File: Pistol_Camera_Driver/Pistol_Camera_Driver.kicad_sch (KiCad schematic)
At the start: 3 parts

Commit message: v0.2 Circuit has been complemented
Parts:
- added C? (x10): C, symbol Device:C
- added D? (x2): WHITE_LED, symbol Device:LED
- added D? (x2): UV_LED, symbol Device:LED
- added J? (x5): Screw_Terminal_01x02, symbol Connector:Screw_Terminal_01x02
- added J?: Screw_Terminal_01x03, symbol Connector:Screw_Terminal_01x03
- added J?: Conn_01x08, symbol Connector_Generic:Conn_01x08
- added M?: Fan, symbol Motor:Fan
- added R? (x15): R, Resistor_SMD:R_0603_1608Metric_Pad0.98x0.95mm_HandSolder, symbol Device:R
- added U?: LM7805_TO220, Package_TO_SOT_THT:TO-220-3_Vertical, symbol Regulator_Linear:LM7805_TO220
- added U?: LM317_TO-263, Package_TO_SOT_SMD:TO-263-2, symbol Regulator_Linear:LM317_TO-263
- added U? (x2): LDD-700L, Converter_DCDC:Converter_DCDC_Murata_NCS1SxxxxSC_THT, symbol Converter_DCDC:NCS1S1203SC
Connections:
- net GND: now reaches U?.13 (GND)
- net GND: now also U?.19 (GP14), U?.21 (GND), U?.21 (GND), U?.23 (GND), U?.25 (GND), U?.25 (GND), U?.28 (GND), U?.3 (GND), U?.33 (AGND), U?.38 (GND), U?.8 (GND), C?.2, C?.2, C?.2, C?.2, J?.2 (Pin_2), J?.2 (Pin_2), J?.2 (Pin_2), J?.3 (Pin_3), M?.2 (-), R?.1, R?.1, R?.1, R?.1, R?.1, R?.1, R?.1, R?.1, R?.2, R?.2, U?.1 (-VIN), U?.1 (-VIN), U?.2 (GND)
- net +5V: now reaches U?.39 (VSYS)
- net +5V: now also C?.1, C?.1, U?.3 (VI), U?.3 (VO)
- net Strobe Input: now reaches U?.4 (GP2)
- net Strobe Input: now also J?.1 (Pin_1)
- net PWM_UV: now reaches U?.7 (GP5/SCL)
- net PWM_UV: now also J?.1 (Pin_1), R?.1, U?.3 (Control)
- net PWM_WHITE: now reaches U?.9 (GP6)
- net PWM_WHITE: now also J?.2 (Pin_2), U?.3 (Control)
- net MOTORS_nSLEEP: now reaches U?.1 (nSLEEP)
- net MOTORS_nSLEEP: now also U?.1 (nSLEEP), R?.2, R?.2
- net nEN1: now reaches U?.10 (nENBL)
- net STEP1: now reaches U?.11 (STEP)
- net DIR1: now reaches U?.12 (DIR)
- net M0_1: now reaches U?.13 (M0)
- net M1_1: now reaches U?.14 (M1)
- net at U?.15 (CONFIG): now also U?.20 (VINT) (x2)
- net at U?.16 (nFAULT): now also R?.2 (x2)
- net +3V3: now reaches U?.18 (VM)
- net +3V3: now also U?.18 (VM), U?.19 (VM), U?.19 (VM), C?.1, R?.1, R?.1, R?.1, R?.1, R?.1, U?.2 (VO)
- net at U?.2 (BDECAY): now also R?.2 (x2)
- net at U?.22 (AVREF): now also U?.23 (BVREF), U?.24 (VREFO) (x2)
- net at U?.3 (ADECAY): now also R?.2 (x2)
- net AOUT1_1: now reaches U?.4 (AOUT1)
- net at U?.5 (AISEN): now also R?.2 (x2)
- net AOUT2_1: now reaches U?.6 (AOUT2)
- net BOUT2_1: now reaches U?.7 (BOUT2)
- net at U?.8 (BISEN): now also R?.2 (x2)
- net BOUT1_2: now reaches U?.9 (BOUT1)
- net BOUT1_2: now also U?.9 (BOUT1)
- net nEN2: now reaches U?.10 (nENBL)
- net STEP2: now reaches U?.11 (STEP)
- net DIR2: now reaches U?.12 (DIR)
- net M0_2: now reaches U?.13 (M0)
- net M1_2: now reaches U?.14 (M1)
- net AOUT1_2: now reaches U?.4 (AOUT1)
- net AOUT2_2: now reaches U?.6 (AOUT2)
- net BOUT2_2: now reaches U?.7 (BOUT2)
- new net: D?.2 (A), J?.1 (Pin_1), U?.6 (+VOUT) (x2)
- new net: D?.1 (K), J?.2 (Pin_2), U?.7 (-VOUT) (x2)
- new net: D?.1 (K), D?.2 (A) (x2)
- new net: R?.1, R?.2, U?.1 (ADJ)
- new net +12V: C?.1, J?.1 (Pin_1), J?.1 (Pin_1), M?.1 (+), U?.1 (VI), U?.2 (+VIN), U?.2 (+VIN)
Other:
- moved on the sheet: U?

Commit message: v0.3 Circuit except the joystick has been completed
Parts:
- added C? (x2): C_Polarized, symbol Device:C_Polarized
- added J?: Conn_01x04_Female, Connector_PinSocket_2.54mm:PinSocket_1x04_P2.54mm_Vertical, symbol Connector:Conn_01x04_Female
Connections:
- net +3V3: now also C?.1, C?.2, C?.2, C?.2, C?.1, C?.1
- net +5V: now also J?.1 (Pin_1)
- net AOUT1_1: now also J?.4 (Pin_4)
- net AOUT1_2: now also J?.2 (Pin_2)
- net AOUT2_1: now also J?.3 (Pin_3)
- net AOUT2_2: now also J?.1 (Pin_1)
- net BOUT1_1: now also J?.5 (Pin_5), U?.9 (BOUT1)
- net BOUT1_2: now also J?.8 (Pin_8); no longer U?.9 (BOUT1)
- net BOUT2_1: now also J?.6 (Pin_6)
- net BOUT2_2: now also J?.7 (Pin_7)
- net DIR1: now also U?.17 (GP13)
- net DIR2: now also U?.24 (GP18/SCK)
- net GND: now also C?.1, C?.2, C?.2, C?.2, U?.18 (GND), C?.2, C?.2, J?.4 (Pin_4); no longer U?.19 (GP14)
- net M0_1: now also U?.19 (GP14)
- net M0_2: now also U?.22 (GP17/CS)
- net M1_1: now also U?.20 (GP15)
- net M1_2: now also U?.21 (GP16/MISO)
- net MOTORS_nSLEEP: now also U?.14 (GP10)
- net STEP1: now also U?.16 (GP12)
- net STEP2: now also U?.25 (GP19/MOSI)
- net nEN1: now also U?.15 (GP11)
- net nEN2: now also U?.26 (GP20)
- net TRIG: now reaches U?.10 (GP7)
- net TRIG: now also J?.2 (Pin_2)
- net ECHO: now reaches U?.11 (GP8)
- net ECHO: now also J?.3 (Pin_3)
- net at U?.15 (CONFIG), U?.20 (VINT): now also C?.1 (x2)
- net at U?.17 (VCP): now also C?.1 (x2)
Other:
- moved on the sheet: C?

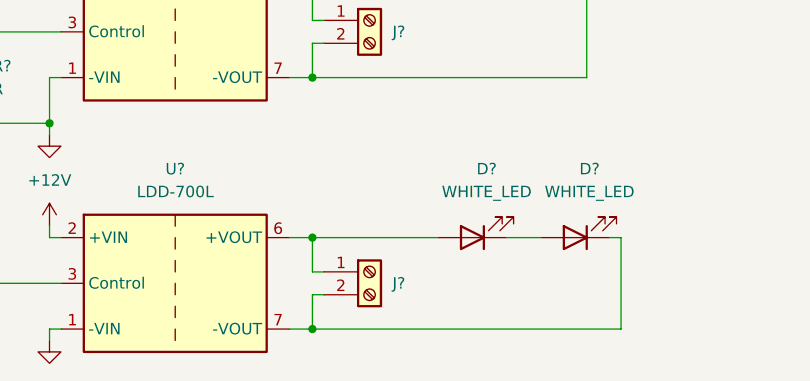
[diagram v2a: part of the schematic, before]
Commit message: v0.4 Footprints of DRV & RPI have been added
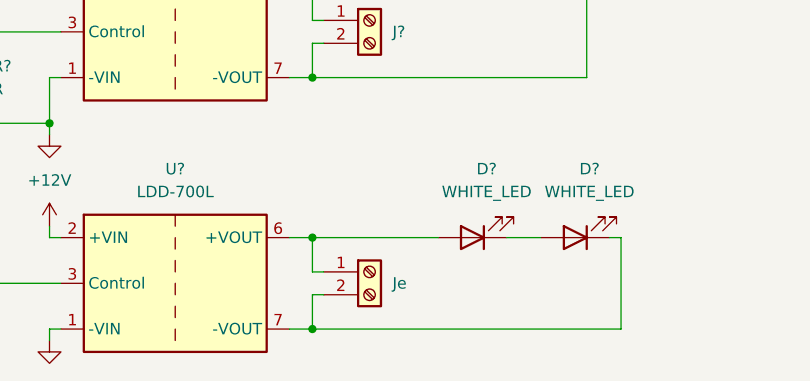
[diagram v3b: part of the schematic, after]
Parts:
- J? (x4): footprint (none) -> Connector_PinSocket_2.54mm:PinSocket_1x02_P2.54mm_Vertical
- Je: renamed from J?; footprint (none) -> Connector_PinSocket_2.54mm:PinSocket_1x02_P2.54mm_Vertical
- U?: footprint (none) -> Shield_Emergent:Raspberry Pi Pico
- U? (x2): footprint (none) -> Shield_Emergent:DRV8834PWP
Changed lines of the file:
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@@
     (property "Reference" "U?" (id 0) (at 134.62 21.59 0))
     (property "Value" "Raspberri_Pi_Pico" (id 1) (at 134.62 24.13 0))
-    (property "Footprint" "" (id 2) (at 130.81 39.37 0)
+    (property "Footprint" "Shield_Emergent:Raspberry Pi Pico" (id 2) (at 130.81 39.37 0)
       (effects (font (size 1.27 1.27)) hide)
     )
@@
       (effects (font (size 1.27 1.27)) hide)
     )
-    (property "Footprint" "" (id 2) (at 35.56 34.29 0)
+    (property "Footprint" "Connector_PinSocket_2.54mm:PinSocket_1x02_P2.54mm_Vertical" (id 2) (at 35.56 34.29 0)
       (effects (font (size 1.27 1.27)) hide)
     )
@@
       (effects (font (size 1.27 1.27)) (justify left) hide)
     )
-    (property "Footprint" "" (id 2) (at 130.81 142.24 0)
+    (property "Footprint" "Connector_PinSocket_2.54mm:PinSocket_1x02_P2.54mm_Vertical" (id 2) (at 130.81 142.24 0)
       (effects (font (size 1.27 1.27)) hide)
     )
@@
       (effects (font (size 1.27 1.27)) (justify left) hide)
     )
-    (property "Footprint" "" (id 2) (at 41.91 73.66 0)
+    (property "Footprint" "Connector_PinSocket_2.54mm:PinSocket_1x02_P2.54mm_Vertical" (id 2) (at 41.91 73.66 0)
       (effects (font (size 1.27 1.27)) hide)
     )
@@
       (effects (font (size 1.27 1.27)) hide)
     )
-    (property "Footprint" "" (id 2) (at 35.56 17.78 0)
+    (property "Footprint" "Connector_PinSocket_2.54mm:PinSocket_1x02_P2.54mm_Vertical" (id 2) (at 35.56 17.78 0)
       (effects (font (size 1.27 1.27)) hide)
     )
@@
   (symbol (lib_id "Connector:Screw_Terminal_01x02") (at 130.81 170.18 0) (unit 1)
     (in_bom yes) (on_board yes) (fields_autoplaced)
-    (property "Reference" "J?" (id 0) (at 133.35 171.4499 0)
+    (property "Reference" "Je" (id 0) (at 133.35 171.4499 0)
       (effects (font (size 1.27 1.27)) (justify left))
     )
@@
       (effects (font (size 1.27 1.27)) (justify left) hide)
     )
-    (property "Footprint" "" (id 2) (at 130.81 170.18 0)
+    (property "Footprint" "Connector_PinSocket_2.54mm:PinSocket_1x02_P2.54mm_Vertical" (id 2) (at 130.81 170.18 0)
       (effects (font (size 1.27 1.27)) hide)
     )
@@
     (property "Reference" "U?" (id 0) (at 208.28 17.78 0))
     (property "Value" "DRV8834PWP" (id 1) (at 208.28 20.32 0))
-    (property "Footprint" "" (id 2) (at 208.28 29.21 0)
+    (property "Footprint" "Shield_Emergent:DRV8834PWP" (id 2) (at 208.28 29.21 0)
       (effects (font (size 1.27 1.27)) hide)
     )
@@
     (property "Reference" "U?" (id 0) (at 208.28 63.5 0))
     (property "Value" "DRV8834PWP" (id 1) (at 208.28 66.04 0))
-    (property "Footprint" "" (id 2) (at 208.28 74.93 0)
+    (property "Footprint" "Shield_Emergent:DRV8834PWP" (id 2) (at 208.28 74.93 0)
       (effects (font (size 1.27 1.27)) hide)
     )
@@
     )
     (path "/38409648-ebc8-4a2e-a61d-bd50b40af8be"
-      (reference "J?") (unit 1) (value "Screw_Terminal_01x02") (footprint "")
+      (reference "J?") (unit 1) (value "Screw_Terminal_01x02") (footprint "Connector_PinSocket_2.54mm:PinSocket_1x02_P2.54mm_Vertical")
     )
     (path "/3fe122b5-ed55-46b8-b1be-4f5727f45b58"
-      (reference "J?") (unit 1) (value "Screw_Terminal_01x02") (footprint "")
+      (reference "J?") (unit 1) (value "Screw_Terminal_01x02") (footprint "Connector_PinSocket_2.54mm:PinSocket_1x02_P2.54mm_Vertical")
     )
     (path "/44be599c-d15a-4294-ab21-4afeb3fc161c"
-      (reference "J?") (unit 1) (value "Screw_Terminal_01x02") (footprint "")
+      (reference "J?") (unit 1) (value "Screw_Terminal_01x02") (footprint "Connector_PinSocket_2.54mm:PinSocket_1x02_P2.54mm_Vertical")
     )
     (path "/705b3455-f7a9-4e6e-b7ce-8fbc52687066"
-      (reference "J?") (unit 1) (value "Screw_Terminal_01x02") (footprint "")
-    )
-    (path "/7fabe294-0d39-4dd3-9c89-852e9ec4a980"
-      (reference "J?") (unit 1) (value "Screw_Terminal_01x02") (footprint "")
+      (reference "J?") (unit 1) (value "Screw_Terminal_01x02") (footprint "Connector_PinSocket_2.54mm:PinSocket_1x02_P2.54mm_Vertical")
     )
     (path "/9999b061-9827-4d4d-9942-f86641ba16f3"
@@
       (reference "J?") (unit 1) (value "Conn_01x08") (footprint "")
     )
+    (path "/7fabe294-0d39-4dd3-9c89-852e9ec4a980"
+      (reference "Je") (unit 1) (value "Screw_Terminal_01x02") (footprint "Connector_PinSocket_2.54mm:PinSocket_1x02_P2.54mm_Vertical")
+    )
     (path "/bc36b4a0-9a30-45d1-9250-349a6006bb74"
       (reference "M?") (unit 1) (value "Fan") (footprint "")
@@
     )
     (path "/28feda8c-5340-47e2-a692-b05f1373aa2a"
-      (reference "U?") (unit 1) (value "Raspberri_Pi_Pico") (footprint "")
+      (reference "U?") (unit 1) (value "Raspberri_Pi_Pico") (footprint "Shield_Emergent:Raspberry Pi Pico")
     )
     (path "/3fd05627-b166-47c3-bddd-c847d3ea980a"
@@
     )
     (path "/92e19121-3851-4086-a290-24fa3a41bdfc"
-      (reference "U?") (unit 1) (value "DRV8834PWP") (footprint "")
+      (reference "U?") (unit 1) (value "DRV8834PWP") (footprint "Shield_Emergent:DRV8834PWP")
     )
     (path "/a124d49e-6423-4e02-bdf9-ca38776e7762"
-      (reference "U?") (unit 1) (value "DRV8834PWP") (footprint "")
+      (reference "U?") (unit 1) (value "DRV8834PWP") (footprint "Shield_Emergent:DRV8834PWP")
     )
     (path "/b63c9d7a-0f35-49f7-90f5-16af5eacab9f"

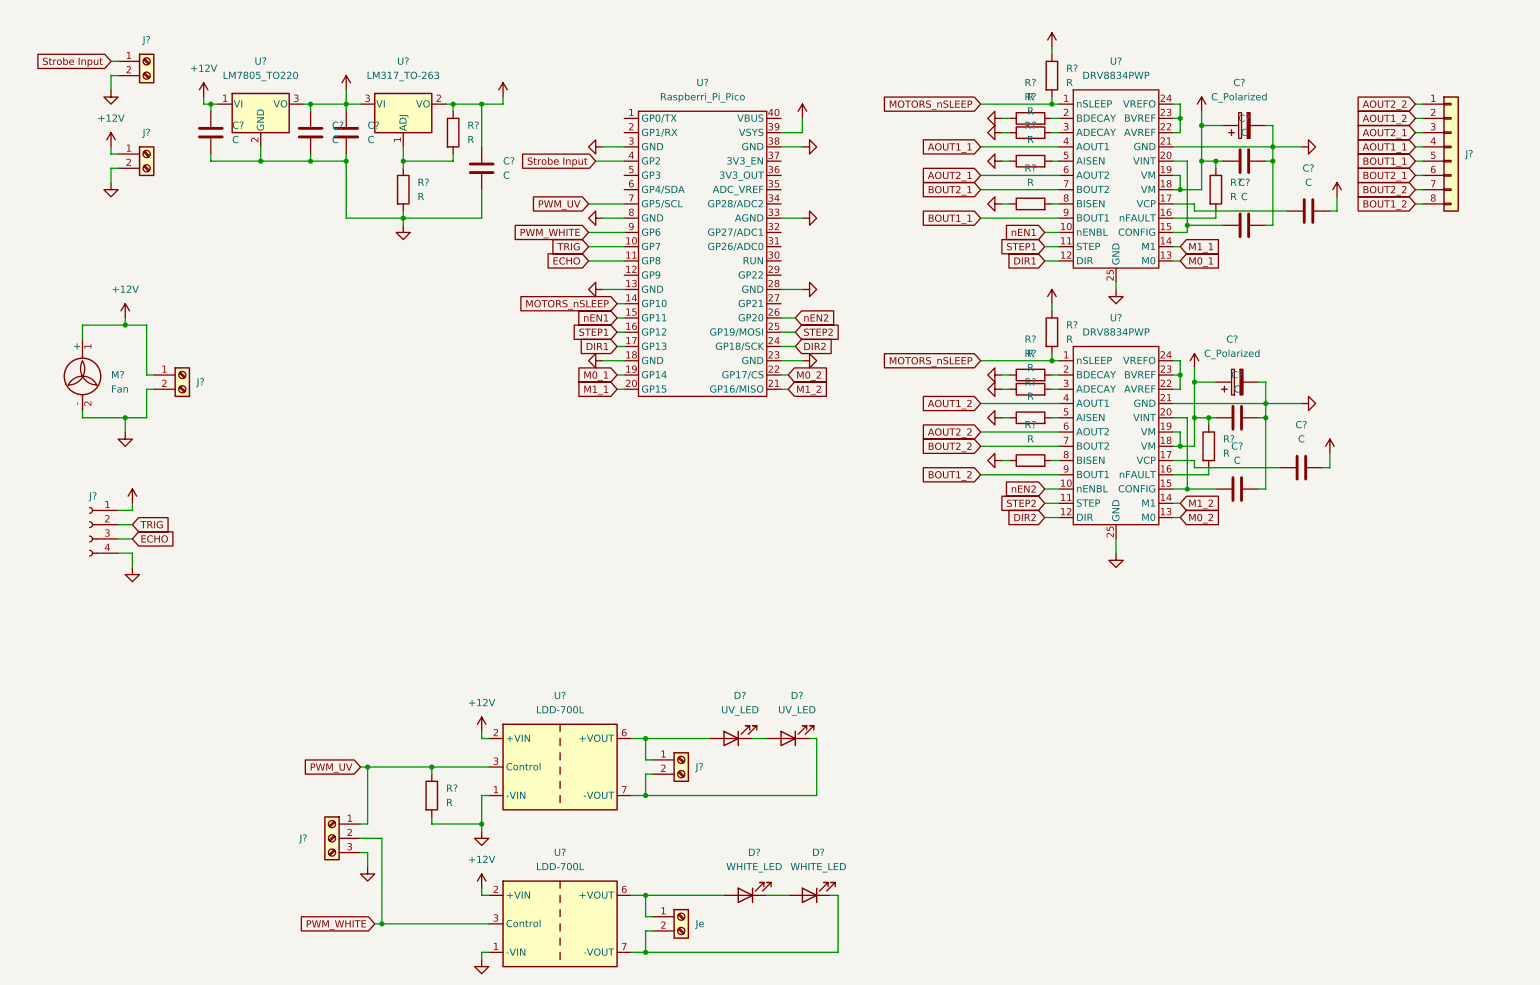
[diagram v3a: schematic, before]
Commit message: v0.5 Joystick has been added
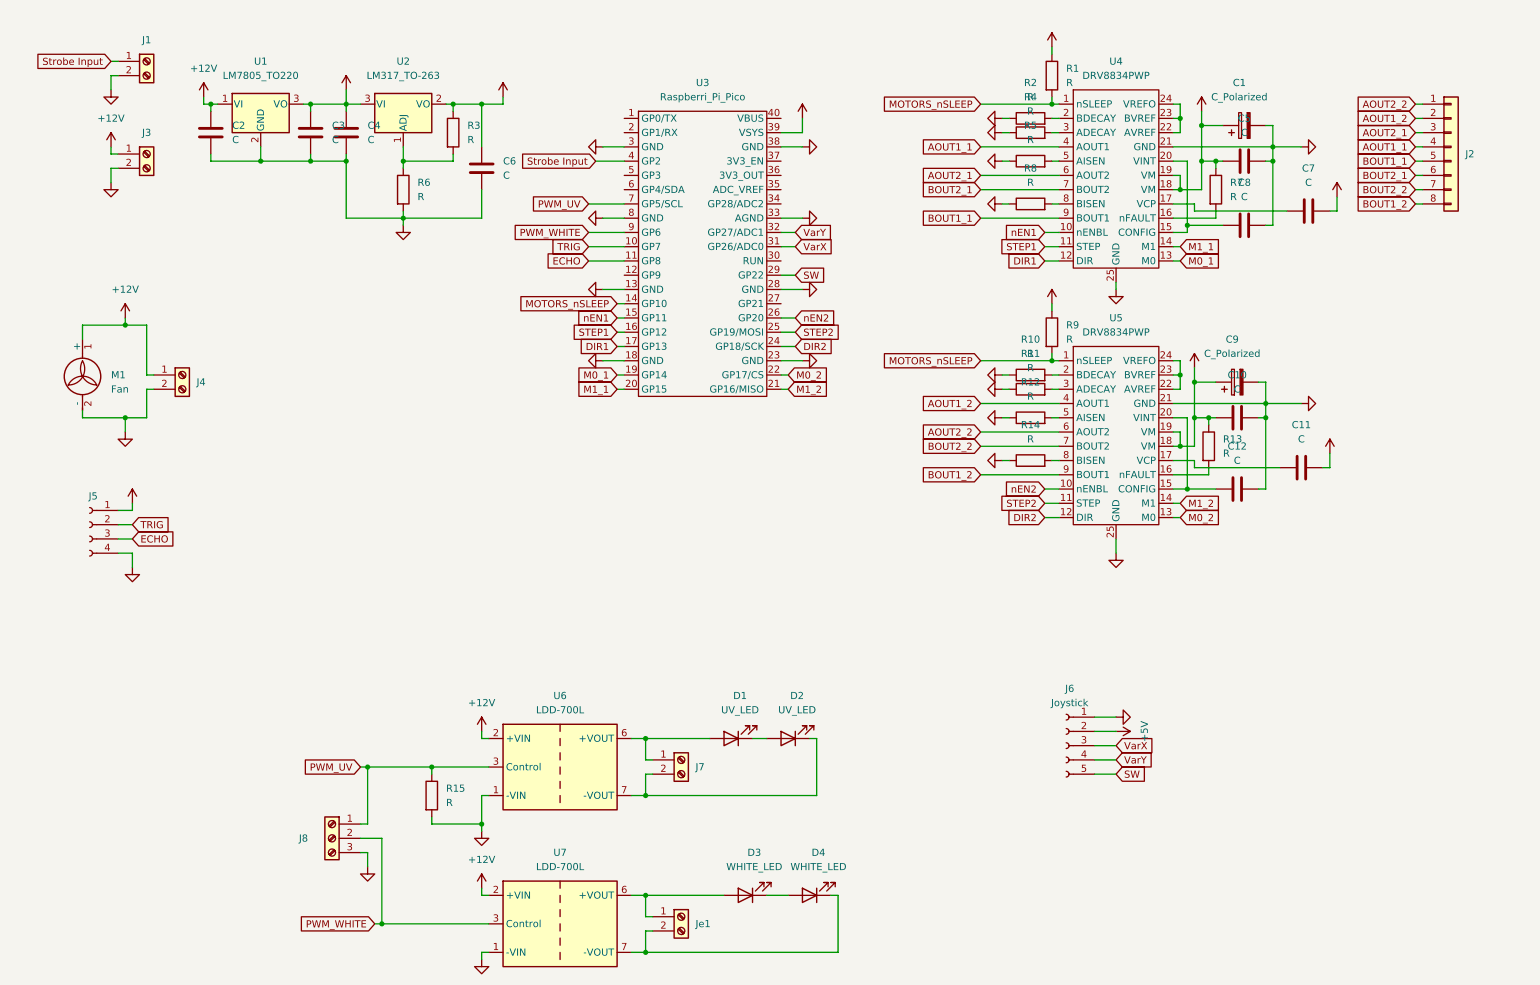
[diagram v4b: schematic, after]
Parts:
- added J6: Joystick, Connector_PinSocket_2.54mm:PinSocket_1x05_P2.54mm_Vertical, symbol Connector:Conn_01x05_Female
- J2: renamed from J?; footprint (none) -> Connector_PinSocket_1.27mm:PinSocket_1x08_P1.27mm_Vertical
- gave numbers to parts that had none: 45
- renumbered Je to Je1
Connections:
- net +5V: now also J6.2 (Pin_2)
- net GND: now also J6.1 (Pin_1)
- net SW: now reaches U3.29 (GP22)
- net SW: now also J6.5 (Pin_5)
- net VarX: now reaches U3.31 (GP26/ADC0)
- net VarX: now also J6.3 (Pin_3)
- net VarY: now reaches U3.32 (GP27/ADC1)
- net VarY: now also J6.4 (Pin_4)

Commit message: v0.6 All the elements have been created
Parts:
- removed U6, U7: LDD-700L, Converter_DCDC:Converter_DCDC_Murata_NCS1SxxxxSC_THT, symbol Converter_DCDC:NCS1S1203SC
- added Q1: IRLML6402, Package_TO_SOT_SMD:SOT-23, symbol Transistor_FET:IRLML6402
- added R15: R, Resistor_SMD:R_0603_1608Metric_Pad0.98x0.95mm_HandSolder, symbol Device:R
- added U6, U7: LDD-700L, Shield_Emergent:LDD-700L, symbol Shield_Emergent:LDD-700L
- C1, C9: footprint (none) -> Capacitor_THT:CP_Radial_D6.3mm_P2.50mm
- C10, C11, C12, C2, C3, C4, C5, C6, C7, C8: footprint (none) -> Capacitor_SMD:C_0603_1608Metric_Pad1.08x0.95mm_HandSolder
- J8: footprint (none) -> Connector_PinSocket_2.54mm:PinSocket_1x03_P2.54mm_Vertical
- renumbered R15 to R16
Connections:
- net +12V: now also U6.1 (Vin+), U7.1 (Vin+)
- net +3V3: now also J6.2 (Pin_2)
- net +5V: now also Q1.2 (S), R15.2; no longer J6.2 (Pin_2)
- net GND: now also U6.3 (Vin-), U7.3 (Vin-)
- net PWM_UV: now also Q1.1 (G), R15.1; no longer R16.1
- net PWM_WHITE: now also U7.2 (PWM)
- net at D1.2 (A), J7.1 (Pin_1): now also U6.5 (Vout+)
- net at D2.1 (K), J7.2 (Pin_2): now also U6.4 (Vout-)
- net at D3.2 (A), Je1.1 (Pin_1): now also U7.5 (Vout+)
- net at D4.1 (K), Je1.2 (Pin_2): now also U7.4 (Vout-)
- new net: Q1.3 (D), R16.1, U6.2 (PWM)
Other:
- moved on the sheet: J8, R16
